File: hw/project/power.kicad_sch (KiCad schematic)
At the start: 22 parts, among them Q1 SQM50061EL_GE3, Q2 SQM50061EL_GE3, U4 LMR51610XDBVR

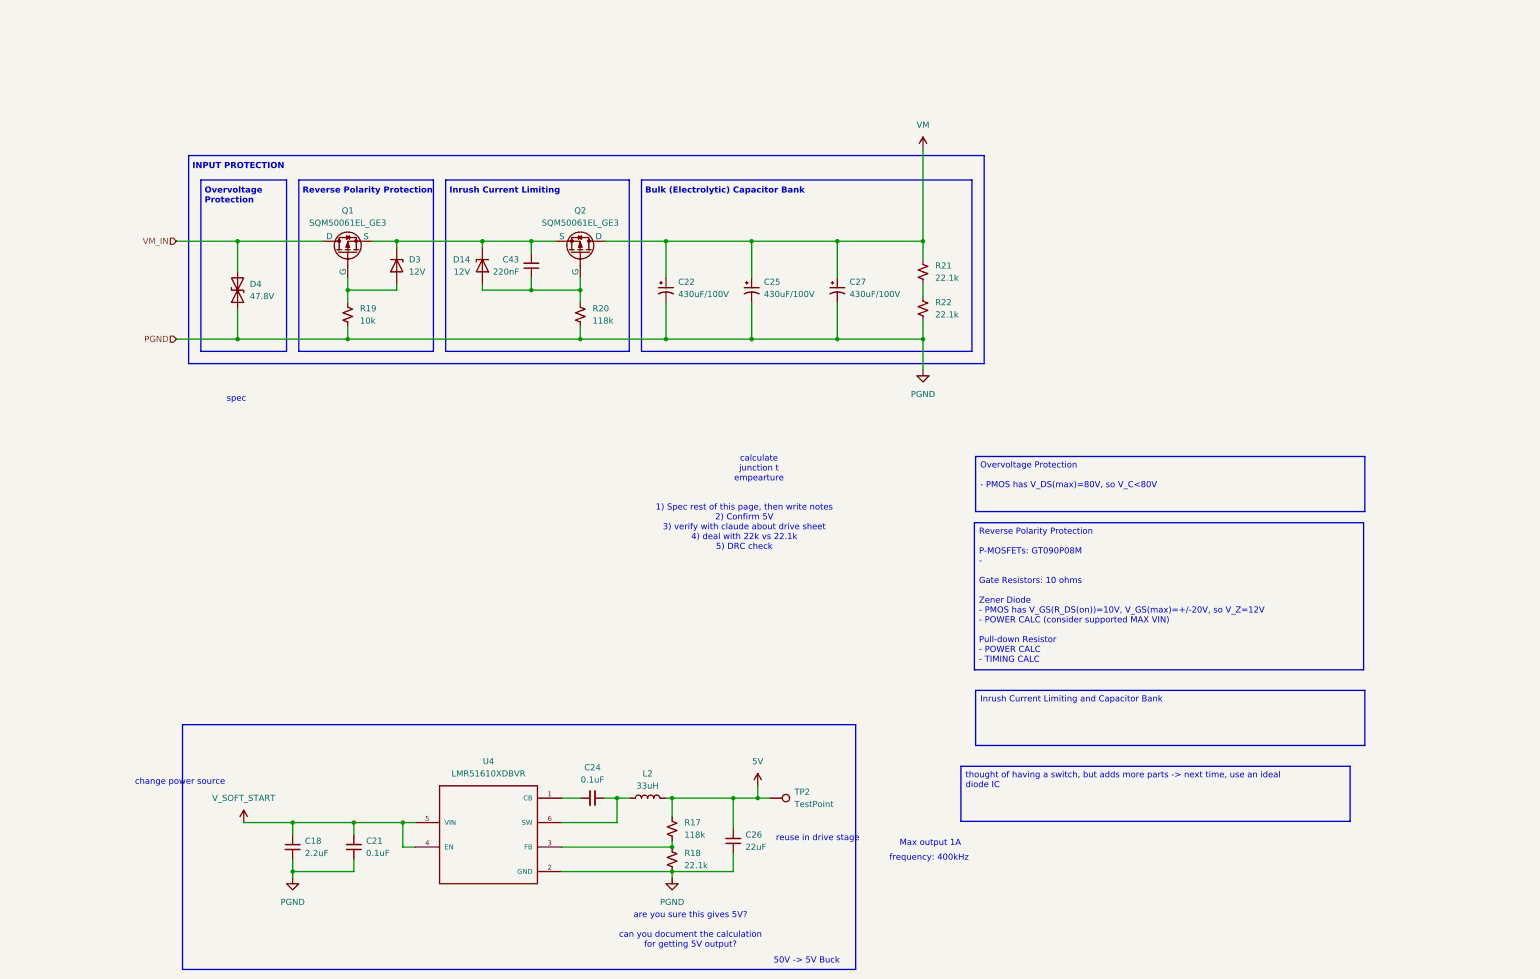
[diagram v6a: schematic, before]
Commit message: Spec input protection
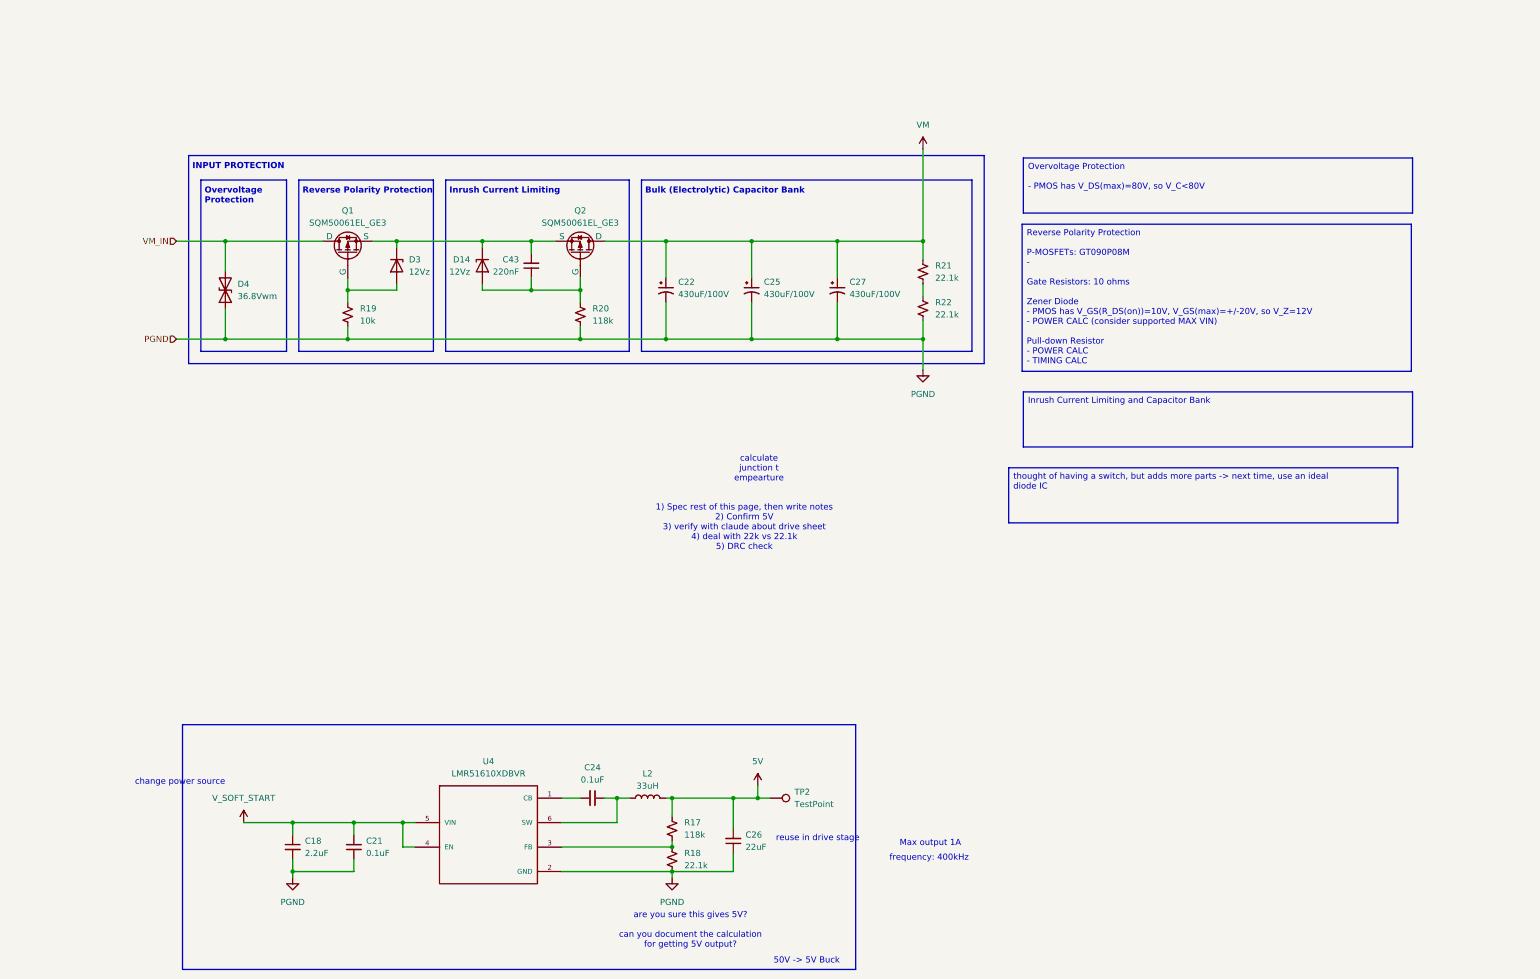
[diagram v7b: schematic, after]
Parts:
- D14, D3: value 12V -> 12Vz
- D4: value 47.8V -> 36.8Vwm; footprint (none) -> Diode_SMD:D_SMB
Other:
- note removed: "spec"
- moved on the sheet: D4
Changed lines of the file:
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@@
-		)
-	)
-	(text "spec"
-		(exclude_from_sim no)
-		(at 32.766 73.406 0)
-		(effects
-			(font
-				(size 1.27 1.27)
-				(color 255 4 4 1)
-			)
 		)
 	)
@@
 	(text_box "Inrush Current Limiting and Capacitor Bank\n\n\n"
 		(exclude_from_sim no)
-		(at 186.182 133.858 0)
+		(at 196.088 71.9092 0)
 		(size 80.772 11.4299)
 		(margins 0.9525 0.9525 0.9525 0.9525)
@@
 	(text_box "Overvoltage Protection\n\n- PMOS has V_DS(max)=80V, so V_C<80V"
 		(exclude_from_sim no)
-		(at 186.182 85.3168 0)
+		(at 196.088 23.368 0)
 		(size 80.772 11.4299)
 		(margins 0.9525 0.9525 0.9525 0.9525)
@@
 	(text_box "Reverse Polarity Protection\n\nP-MOSFETs: GT090P08M\n- \n\nGate Resistors: 10 ohms\n\nZener Diode\n- PMOS has V_GS(R_DS(on))=10V, V_GS(max)=+/-20V, so V_Z=12V\n- POWER CALC (consider supported MAX VIN)\n\nPull-down Resistor\n- POWER CALC\n- TIMING CALC"
 		(exclude_from_sim no)
-		(at 185.928 99.06 0)
+		(at 195.834 37.1112 0)
 		(size 80.772 30.5285)
 		(margins 0.9525 0.9525 0.9525 0.9525)
@@
 	(text_box "thought of having a switch, but adds more parts -> next time, use an ideal diode IC"
 		(exclude_from_sim no)
-		(at 183.134 149.606 0)
+		(at 193.04 87.6572 0)
 		(size 80.772 11.4299)
 		(margins 0.9525 0.9525 0.9525 0.9525)
@@
 	)
 	(junction
-		(at 33.02 60.96)
+		(at 30.48 60.96)
 		(diameter 0)
 		(color 0 0 0 0)
@@
 	)
 	(junction
+		(at 30.48 40.64)
+		(diameter 0)
+		(color 0 0 0 0)
+	)
+	(junction
 		(at 139.7 40.64)
 		(diameter 0)
@@
 	)
 	(junction
-		(at 33.02 40.64)
-		(diameter 0)
-		(color 0 0 0 0)
-	)
-	(junction
 		(at 121.92 40.64)
 		(diameter 0)
@@
 	(wire
 		(pts
+			(xy 30.48 60.96) (xy 55.88 60.96)
+		)
+		(stroke
+			(width 0)
+			(type default)
+		)
+	)
+	(wire
+		(pts
 			(xy 121.92 40.64) (xy 121.92 48.26)
 		)
@@
 	(wire
 		(pts
-			(xy 20.32 60.96) (xy 33.02 60.96)
+			(xy 20.32 60.96) (xy 30.48 60.96)
 		)
 		(stroke
@@
 	(wire
 		(pts
-			(xy 20.32 40.64) (xy 33.02 40.64)
+			(xy 20.32 40.64) (xy 30.48 40.64)
 		)
 		(stroke
@@
 	(wire
 		(pts
-			(xy 33.02 40.64) (xy 33.02 46.99)
-		)
-		(stroke
-			(width 0)
-			(type default)
-		)
-	)
-	(wire
-		(pts
-			(xy 33.02 40.64) (xy 50.8 40.64)
+			(xy 30.48 40.64) (xy 30.48 46.99)
 		)
 		(stroke
@@
 	(wire
 		(pts
-			(xy 33.02 60.96) (xy 55.88 60.96)
-		)
-		(stroke
-			(width 0)
-			(type default)
-		)
-	)
-	(wire
-		(pts
 			(xy 93.98 40.64) (xy 99.06 40.64)
 		)
@@
 	(wire
 		(pts
+			(xy 30.48 40.64) (xy 50.8 40.64)
+		)
+		(stroke
+			(width 0)
+			(type default)
+		)
+	)
+	(wire
+		(pts
 			(xy 139.7 60.96) (xy 175.26 60.96)
 		)
@@
 	(wire
 		(pts
-			(xy 33.02 54.61) (xy 33.02 60.96)
+			(xy 30.48 54.61) (xy 30.48 60.96)
 		)
 		(stroke
@@
 			)
 		)
-		(property "Value" "12V"
+		(property "Value" "12Vz"
 			(at 81.28 46.9899 90)
 			(show_name no)
@@
 	(symbol
 		(lib_id "Device:D_TVS")
-		(at 33.02 50.8 90)
+		(at 30.48 50.8 90)
 		(unit 1)
 		(body_style 1)
@@
 		(fields_autoplaced yes)
 		(property "Reference" "D4"
-			(at 35.56 49.5299 90)
+			(at 33.02 49.5299 90)
 			(show_name no)
 			(do_not_autoplace no)
@@
 			)
 		)
-		(property "Value" "47.8V"
-			(at 35.56 52.0699 90)
+		(property "Value" "36.8Vwm"
+			(at 33.02 52.0699 90)
 			(show_name no)
 			(do_not_autoplace no)
@@
 			)
 		)
-		(property "Footprint" ""
-			(at 33.02 50.8 0)
-			(hide yes)
-			(show_name no)
-			(do_not_autoplace no)
-			(effects
-				(font
-					(size 1.27 1.27)
-				)
-			)
-		)
-		(property "Datasheet" ""
-			(at 33.02 50.8 0)
-			(hide yes)
-			(show_name no)
-			(do_not_autoplace no)
-			(effects
-				(font
-					(size 1.27 1.27)
-				)
-			)
-		)
-		(property "Description" "Bidirectional transient-voltage-suppression diode"
-			(at 33.02 50.8 0)
+		(property "Footprint" "Diode_SMD:D_SMB"
+			(at 30.48 50.8 0)
+			(hide yes)
+			(show_name no)
+			(do_not_autoplace no)
+			(effects
+				(font
+					(size 1.27 1.27)
+				)
+			)
+		)
+		(property "Datasheet" "https://www.digikey.ca/en/products/detail/yageo/P6SMB43CA-AT-TR13/16266003"
+			(at 30.48 50.8 0)
+			(hide yes)
+			(show_name no)
+			(do_not_autoplace no)
+			(effects
+				(font
+					(size 1.27 1.27)
+				)
+			)
+		)
+		(property "Description" "TVS DIODE 36.8VWM 59.3V DO214AA"
+			(at 30.48 50.8 0)
 			(hide yes)
 			(show_name no)
@@
 			)
 		)
-		(property "Value" "12V"
+		(property "Value" "12Vz"
 			(at 68.58 46.9899 90)
 			(show_name no)

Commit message: Write notes for input protection
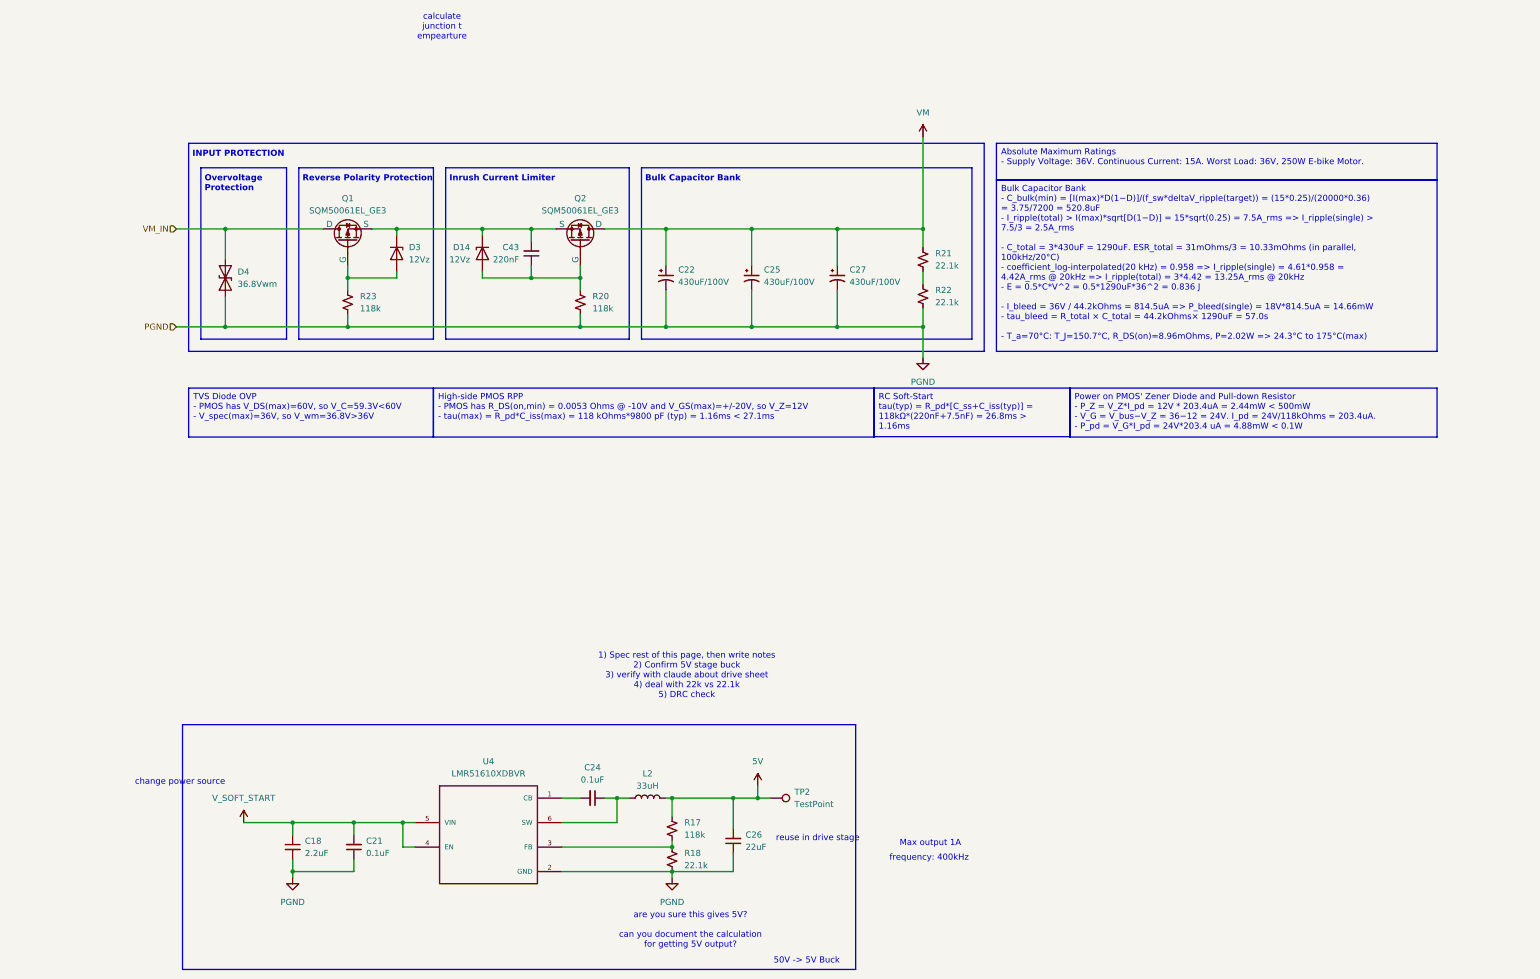
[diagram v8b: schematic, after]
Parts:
- removed R19: 10k, Resistor_SMD:R_0603_1608Metric, symbol Device:R_Small_US
- added R23: 118k, Resistor_SMD:R_0603_1608Metric, symbol Device:R_Small_US
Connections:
- net PGND: now also R23.2
- net at D3.2 (A), Q1.1 (G): now also R23.1
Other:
- note added: "1) Spec rest of this page, then write notes 2) Confirm 5V stage buck 3) verify with claude about drive sheet 4) deal with 22k vs 22.1k 5) DRC check"
- note added: "Bulk Capacitor Bank"
- note added: "Inrush Current Limiter"
- note removed: "1) Spec rest of this page, then write notes 2) Confirm 5V 3) verify with claude about drive sheet 4) deal with 22k vs 22.1k 5) DRC check"
- note removed: "Bulk (Electrolytic) Capacitor Bank"
- note removed: "Inrush Current Limiting"
- moved on the sheet: C22, C25, C27, C43, D14, D3, D4, Q1, Q2, R20, R21, R22
